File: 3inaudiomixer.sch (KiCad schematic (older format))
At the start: 2 parts, among them U1 LF353D, U2 LF353D

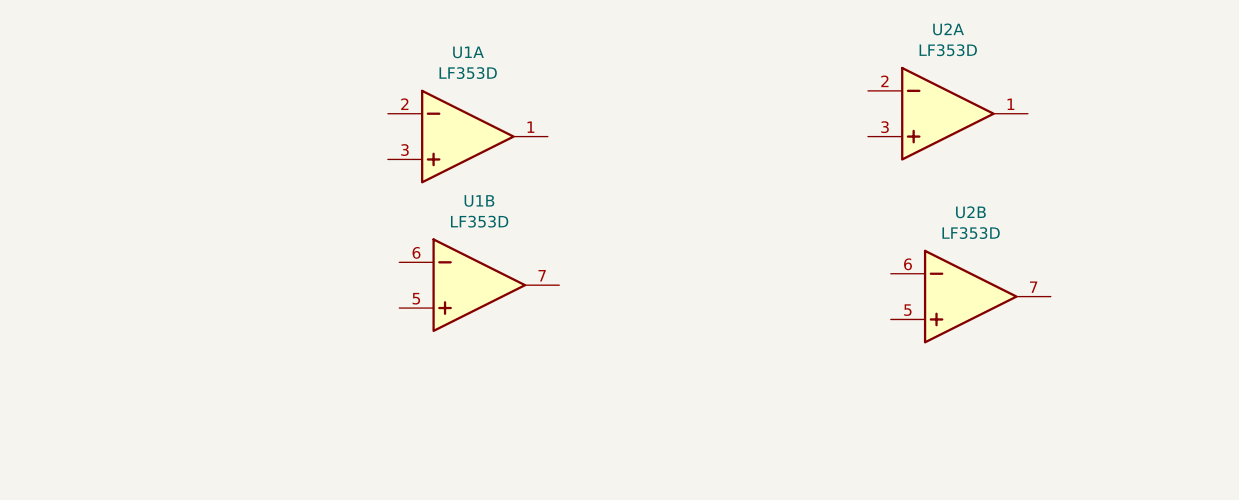
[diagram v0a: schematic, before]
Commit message: some sch components added
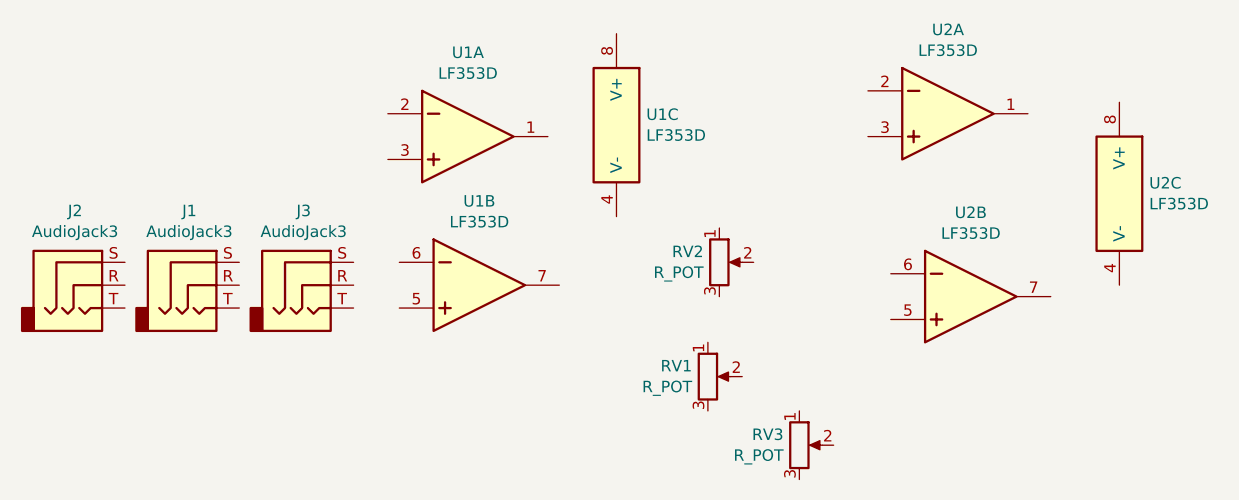
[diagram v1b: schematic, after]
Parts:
- added J1, J2, J3: AudioJack3, Connector_Audio:Jack_3.5mm_CUI_SJ1-3533NG_Horizontal_CircularHoles, symbol Connector:AudioJack3
- added RV1, RV2, RV3: R_POT, Potentiometer_THT:Potentiometer_Omeg_PC16BU_Horizontal, symbol Device:R_POT
- added unit 3 of U1
- added unit 3 of U2
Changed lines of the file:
@@
+	1    0    0    -1
+$EndComp
+$Comp
+L Device:R_POT RV1
+U 1 1 60A9BD08
+P 4800 4300
+F 0 "RV1" H 4731 4346 50  0000 R CNN
+F 1 "R_POT" H 4731 4255 50  0000 R CNN
+F 2 "Potentiometer_THT:Potentiometer_Omeg_PC16BU_Horizontal" H 4800 4300 50  0001 C CNN
+F 3 "~" H 4800 4300 50  0001 C CNN
+	1    4800 4300
+	1    0    0    -1
+$EndComp
+$Comp
+L Device:R_POT RV2
+U 1 1 60A9E345
+P 4850 3800
+F 0 "RV2" H 4781 3846 50  0000 R CNN
+F 1 "R_POT" H 4781 3755 50  0000 R CNN
+F 2 "Potentiometer_THT:Potentiometer_Omeg_PC16BU_Horizontal" H 4850 3800 50  0001 C CNN
+F 3 "~" H 4850 3800 50  0001 C CNN
+	1    4850 3800
+	1    0    0    -1
+$EndComp
+$Comp
+L Device:R_POT RV3
+U 1 1 60A9EA12
+P 5200 4600
+F 0 "RV3" H 5131 4646 50  0000 R CNN
+F 1 "R_POT" H 5131 4555 50  0000 R CNN
+F 2 "Potentiometer_THT:Potentiometer_Omeg_PC16BU_Horizontal" H 5200 4600 50  0001 C CNN
+F 3 "~" H 5200 4600 50  0001 C CNN
+	1    5200 4600
+	1    0    0    -1
+$EndComp
+$Comp
+L Connector:AudioJack3 J2
+U 1 1 60AA760F
+P 2050 3900
+F 0 "J2" H 2032 4225 50  0000 C CNN
+F 1 "AudioJack3" H 2032 4134 50  0000 C CNN
+F 2 "Connector_Audio:Jack_3.5mm_CUI_SJ1-3533NG_Horizontal_CircularHoles" H 2050 3900 50  0001 C CNN
+F 3 "~" H 2050 3900 50  0001 C CNN
+	1    2050 3900
+	1    0    0    -1
+$EndComp
+$Comp
+L Connector:AudioJack3 J1
+U 1 1 60AA8E72
+P 2550 3900
+F 0 "J1" H 2532 4225 50  0000 C CNN
+F 1 "AudioJack3" H 2532 4134 50  0000 C CNN
+F 2 "Connector_Audio:Jack_3.5mm_CUI_SJ1-3533NG_Horizontal_CircularHoles" H 2550 3900 50  0001 C CNN
+F 3 "~" H 2550 3900 50  0001 C CNN
+	1    2550 3900
+	1    0    0    -1
+$EndComp
+$Comp
+L Connector:AudioJack3 J3
+U 1 1 60AA954D
+P 3050 3900
+F 0 "J3" H 3032 4225 50  0000 C CNN
+F 1 "AudioJack3" H 3032 4134 50  0000 C CNN
+F 2 "Connector_Audio:Jack_3.5mm_CUI_SJ1-3533NG_Horizontal_CircularHoles" H 3050 3900 50  0001 C CNN
+F 3 "~" H 3050 3900 50  0001 C CNN
+	1    3050 3900
+	1    0    0    -1
+$EndComp
+$Comp
+L lf353d:LF353D U1
+U 3 1 60AACA7F
+P 4400 3200
+F 0 "U1" H 4530 3246 50  0000 L CNN
+F 1 "LF353D" H 4530 3155 50  0000 L CNN
+F 2 "Package_SO:SOIC-8_3.9x4.9mm_P1.27mm" H 4400 2900 50  0001 C CNN
+F 3 "http://www.ti.com/lit/ds/symlink/lf353.pdf" H 4400 2800 50  0001 C CNN
+F 4 "LF353D" H 4400 2500 50  0001 C CNN "MPN"
+F 5 "TI" H 4400 2600 50  0001 C CNN "Manuf"
+F 6 "TI LF353D" H 4400 2700 50  0001 C CNN "BOM"
+	3    4400 3200
+	1    0    0    -1
+$EndComp
+$Comp
+L lf353d:LF353D U2
+U 3 1 60AAFDA3
+P 6600 3500
+F 0 "U2" H 6730 3546 50  0000 L CNN
+F 1 "LF353D" H 6730 3455 50  0000 L CNN
+F 2 "IPC7351-Nominal:SOIC127P600X175-8" H 6600 3200 50  0001 C CNN
+F 3 "http://www.ti.com/lit/ds/symlink/lf353.pdf" H 6600 3100 50  0001 C CNN
+F 4 "LF353D" H 6600 2800 50  0001 C CNN "MPN"
+F 5 "TI" H 6600 2900 50  0001 C CNN "Manuf"
+F 6 "TI LF353D" H 6600 3000 50  0001 C CNN "BOM"
+	3    6600 3500
 	1    0    0    -1
 $EndComp

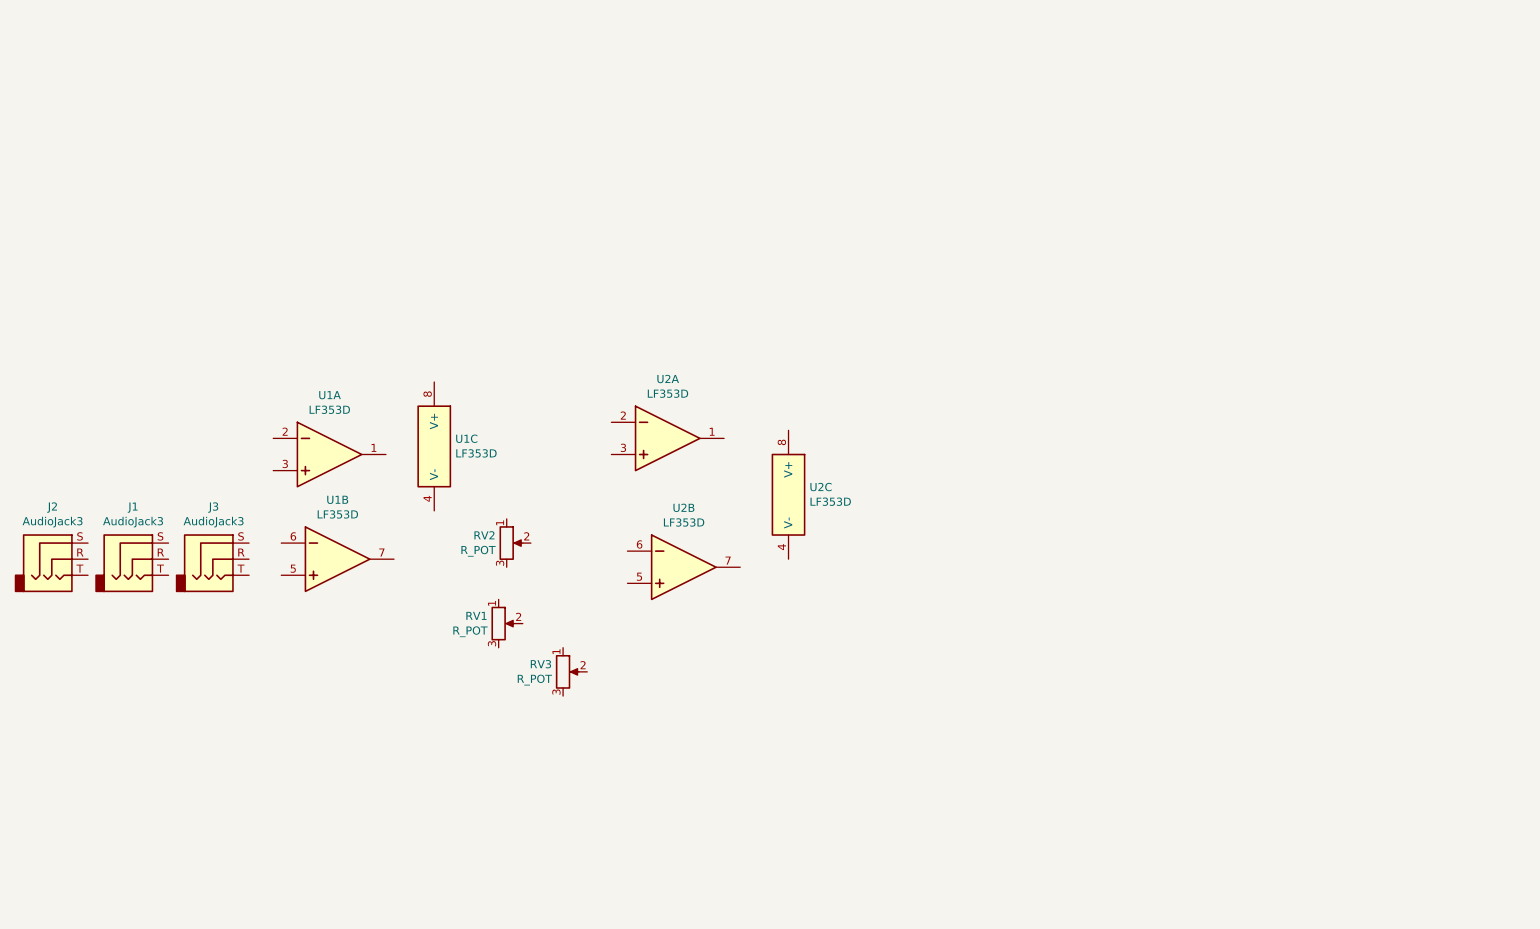
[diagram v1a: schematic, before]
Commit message: almost all components placed
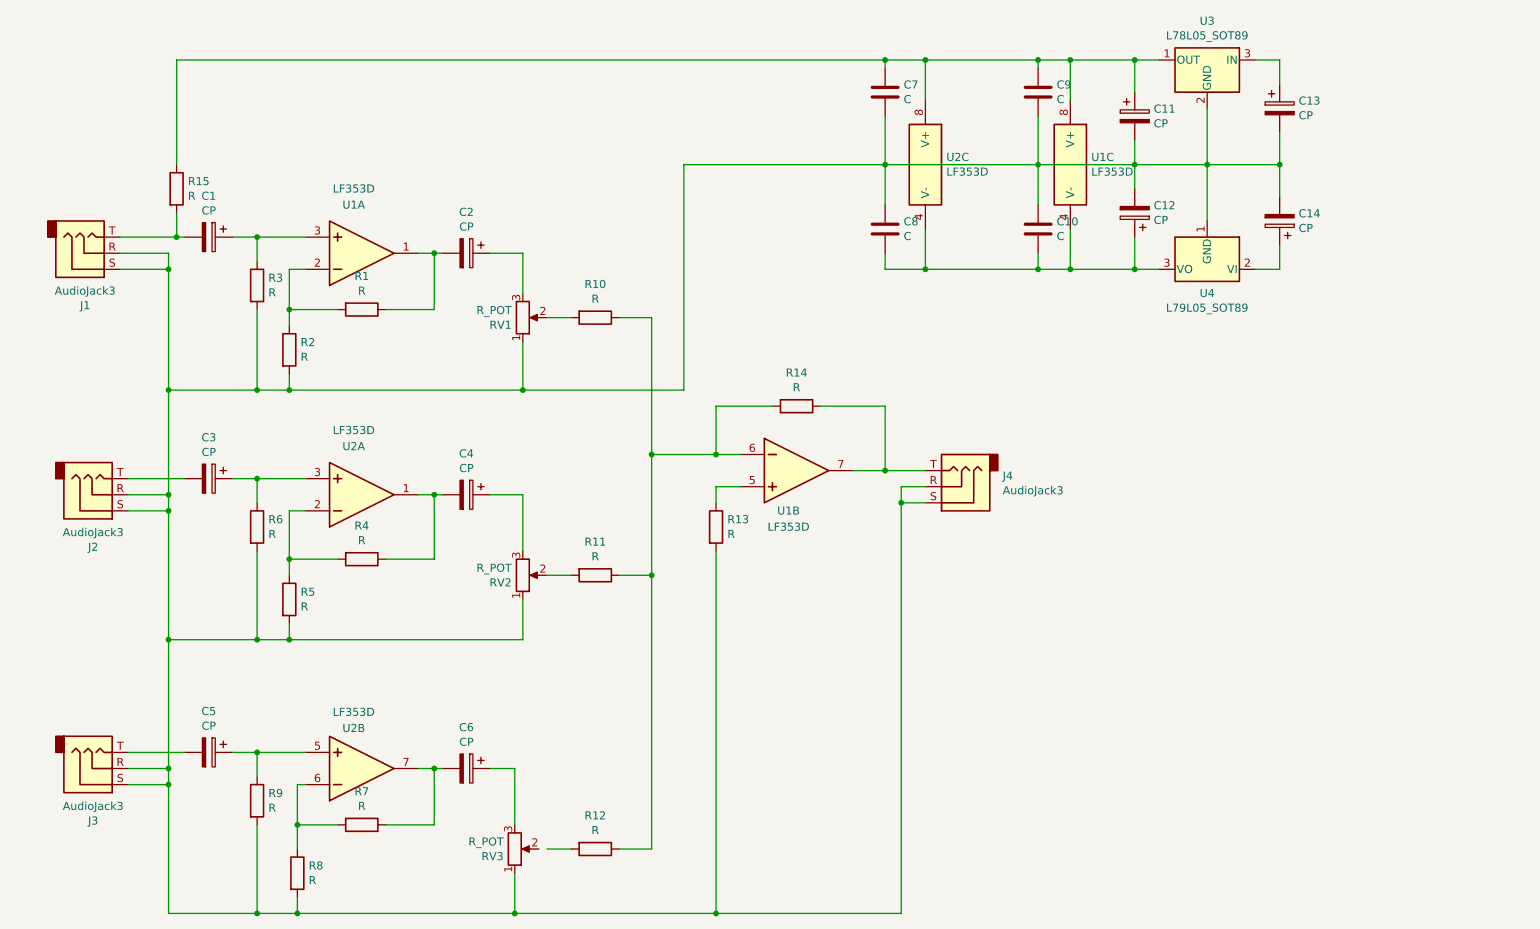
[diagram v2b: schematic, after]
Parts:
- added C1, C2, C3, C4, C5, C6: CP, Capacitor_SMD:C_0805_2012Metric_Pad1.15x1.40mm_HandSolder, symbol Device:CP
- added C10, C7, C8, C9: C, Capacitor_SMD:C_0805_2012Metric_Pad1.15x1.40mm_HandSolder, symbol Device:C
- added C11, C12: CP, Capacitor_SMD:C_1206_3216Metric_Pad1.42x1.75mm_HandSolder, symbol Device:CP
- added C13, C14: CP, Capacitor_SMD:C_Elec_6.3x7.7, symbol Device:CP
- added J4: AudioJack3, symbol Connector:AudioJack3
- added R1, R10, R11, R12, R13, R14, R15, R2, R3, R4, R5, R6, R7, R8, R9: R, Resistor_SMD:R_0805_2012Metric_Pad1.15x1.40mm_HandSolder, symbol Device:R
- added U3: L78L05_SOT89, Package_TO_SOT_SMD:SOT-89-3, symbol Regulator_Linear:L78L05_SOT89
- added U4: L79L05_SOT89, Package_TO_SOT_SMD:SOT-89-3, symbol Regulator_Linear:L79L05_SOT89
- U2: footprint IPC7351-Nominal:SOIC127P600X175-8 -> Package_SO:SOIC-8_3.9x4.9mm_P1.27mm
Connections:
- net at U1.1 (OUT): now also C2.2, R1.1
- net at U1.2 (IN-): now also R1.2, R2.1
- net at U1.3 (IN+): now also C1.1, R3.1
- net at RV1.1: now also J1.R, J1.S, J2.R, J2.S, J3.R, J3.S, RV2.1, RV3.1, C10.1, C11.2, C12.2, C13.2, C14.2, C7.2, C8.1, C9.2, J4.R, J4.S, R13.2, R2.2, R3.2, R5.2, R6.2, R8.2, R9.2, U3.2 (GND), U4.1 (GND)
- net at RV1.2: now also R10.2
- net at RV1.3: now also C2.1
- net at U1.5 (IN+): now also R13.1
- net at U1.6 (IN-): now also R10.1, R11.1, R12.1, R14.2
- net at U1.7 (OUT): now also J4.T, R14.1
- net at U2.1 (OUT): now also C4.2, R4.1
- net at U2.2 (IN-): now also R4.2, R5.1
- net at U2.3 (IN+): now also C3.1, R6.1
- net at U2.5 (IN+): now also C5.1, R9.1
- net at U2.6 (IN-): now also R7.2, R8.1
- net at U2.7 (OUT): now also C6.2, R7.1
- net at RV2.2: now also R11.2
- net at RV2.3: now also C4.1
- net at RV3.3: now also C6.1
- net at J2.T: now also C3.2
- net at J1.T: now also C1.2, R15.2
- net at J3.T: now also C5.2
- net at U1.4 (V-): now also U2.4 (V-), C10.2, C12.1, C8.2, U4.3 (VO)
- net at U1.8 (V+): now also U2.8 (V+), C11.1, C7.1, C9.1, R15.1, U3.1 (OUT)
- new net: C13.1, U3.3 (IN)
- new net: C14.1, U4.2 (VI)
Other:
- moved on the sheet: J1, J2, J3, RV1, RV2, RV3, U1A, U1B, U1C, U2A, U2B, U2C

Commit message: some traces routed
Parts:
- J4: footprint (none) -> Connector_Audio:Jack_3.5mm_CUI_SJ1-3533NG_Horizontal_CircularHoles
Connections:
- net at RV3.2: now also R12.2
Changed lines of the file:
@@
 	5100 4000 5250 4000
-Wire Wire Line
-	5100 5700 5250 5700
 Wire Wire Line
 	5550 2400 5750 2400
@@
 F 0 "J4" H 7370 3383 50  0000 R CNN
 F 1 "AudioJack3" H 7370 3474 50  0000 R CNN
-F 2 "" H 7650 3450 50  0001 C CNN
+F 2 "Connector_Audio:Jack_3.5mm_CUI_SJ1-3533NG_Horizontal_CircularHoles" H 7650 3450 50  0001 C CNN
 F 3 "~" H 7650 3450 50  0001 C CNN
 	1    7650 3450
@@
 	9650 1650 9650 1450
 Connection ~ 9650 1450
+Wire Wire Line
+	5050 5700 5250 5700
 $EndSCHEMATC

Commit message: mounting holes
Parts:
- added J5: Conn_01x03_Female, symbol Connector:Conn_01x03_Female
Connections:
- net at C10.1, C11.2, C12.2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: now also J5.2 (Pin_2)
- net at C13.1, U3.3 (IN): now also J5.1 (Pin_1)
- net at C14.1, U4.2 (VI): now also J5.3 (Pin_3)
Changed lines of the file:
@@
 Wire Wire Line
 	5050 5700 5250 5700
+$Comp
+L Connector:Conn_01x03_Female J5
+U 1 1 60B79D11
+P 10300 1450
+F 0 "J5" H 10328 1476 50  0000 L CNN
+F 1 "Conn_01x03_Female" H 10328 1385 50  0000 L CNN
+F 2 "" H 10300 1450 50  0001 C CNN
+F 3 "~" H 10300 1450 50  0001 C CNN
+	1    10300 1450
+	1    0    0    -1
+$EndComp
+Wire Wire Line
+	9650 1450 10100 1450
+Wire Wire Line
+	9650 2100 10000 2100
+Wire Wire Line
+	10000 2100 10000 1550
+Wire Wire Line
+	10000 1550 10100 1550
+Connection ~ 9650 2100
+Wire Wire Line
+	9650 800  10000 800
+Wire Wire Line
+	10000 800  10000 1350
+Wire Wire Line
+	10000 1350 10100 1350
+Connection ~ 9650 800
 $EndSCHEMATC

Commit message: all traces routed & ground planes
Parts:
- J5: footprint (none) -> TerminalBlock_4Ucon:TerminalBlock_4Ucon_1x03_P3.50mm_Horizontal
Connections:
- net at C13.1, U3.3 (IN): now also J5.3 (Pin_3); no longer J5.1 (Pin_1)
- net at C14.1, U4.2 (VI): now also J5.1 (Pin_1); no longer J5.3 (Pin_3)
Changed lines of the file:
@@
 F 0 "J5" H 10328 1476 50  0000 L CNN
 F 1 "Conn_01x03_Female" H 10328 1385 50  0000 L CNN
-F 2 "" H 10300 1450 50  0001 C CNN
+F 2 "TerminalBlock_4Ucon:TerminalBlock_4Ucon_1x03_P3.50mm_Horizontal" H 10300 1450 50  0001 C CNN
 F 3 "~" H 10300 1450 50  0001 C CNN
 	1    10300 1450
-	1    0    0    -1
+	1    0    0    1
 $EndComp
 Wire Wire Line
-	9650 1450 10100 1450
+	9650 2100 10000 2100
+Connection ~ 9650 2100
 Wire Wire Line
-	9650 2100 10000 2100
+	9650 800  10000 800
+Connection ~ 9650 800
+Wire Wire Line
+	10000 800  10000 1350
+Wire Wire Line
+	10000 1350 10100 1350
 Wire Wire Line
 	10000 2100 10000 1550
 Wire Wire Line
 	10000 1550 10100 1550
-Connection ~ 9650 2100
 Wire Wire Line
-	9650 800  10000 800
-Wire Wire Line
-	10000 800  10000 1350
-Wire Wire Line
-	10000 1350 10100 1350
-Connection ~ 9650 800
+	10100 1450 9650 1450
 $EndSCHEMATC
